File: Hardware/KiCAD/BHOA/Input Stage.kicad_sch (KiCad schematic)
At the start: 15 parts, among them U601 OPA1688, U602 LME49724

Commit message: added outpout relays
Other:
- company: (none) -> C Audio
- title: (none) -> BHOA
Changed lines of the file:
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@@
 (kicad_sch (version 20230121) (generator eeschema)
-  (paper "A5")
+  (paper "A4")
+  (title_block
+    (title "BHOA")
+    (rev "0.1")
+    (company "C Audio")
+    (comment 3 "Balanced Headphone Operationsal Amplifier")
+  )
   (junction (at 126.365 47.625) (diameter 0) (color 0 0 0 0)
   )

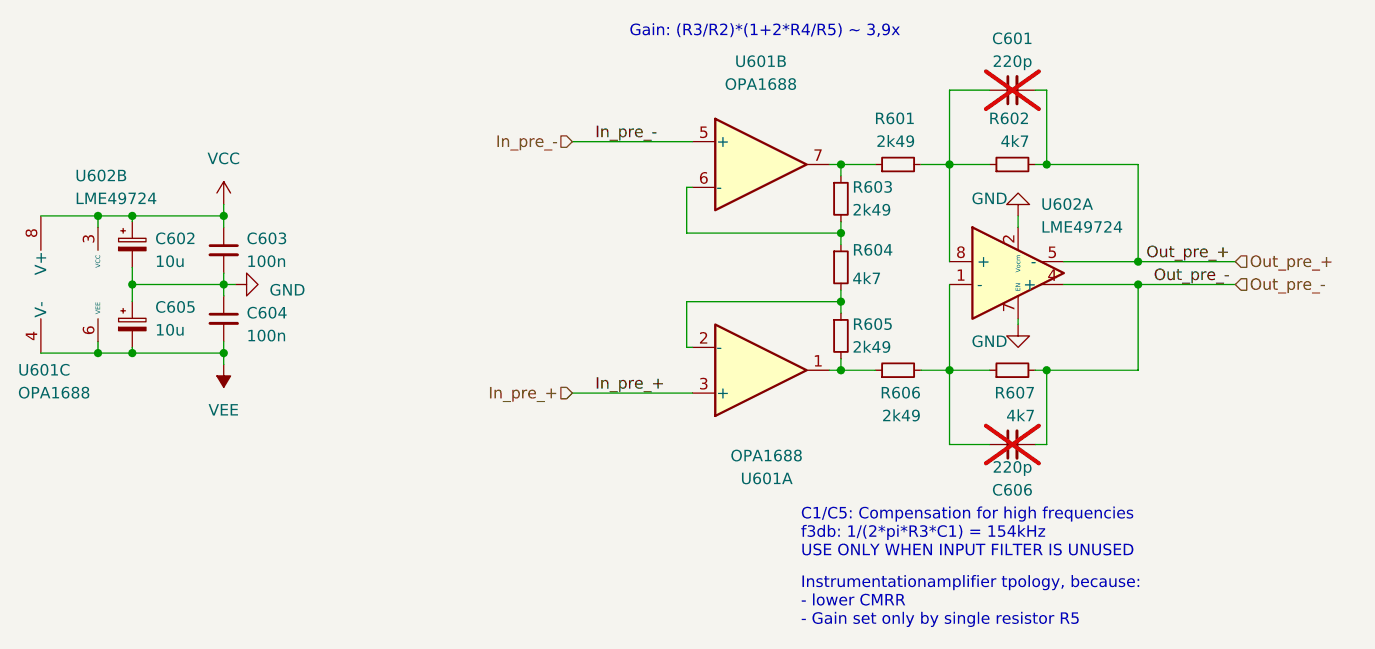
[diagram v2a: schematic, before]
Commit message: Updated PCB with output protection
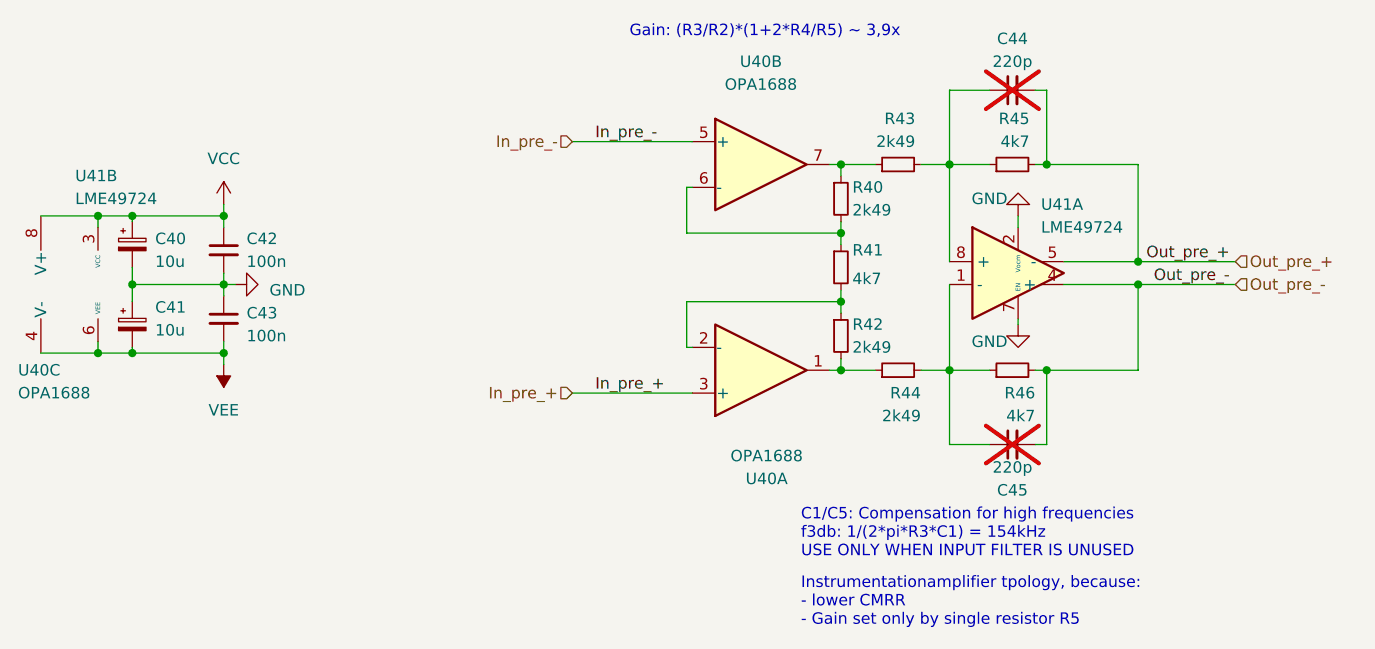
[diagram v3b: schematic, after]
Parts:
- renumbered C602 to C40, C605 to C41, C603 to C42, C604 to C43, C601 to C44, C606 to C45, R603 to R40, R604 to R41, R605 to R42, R601 to R43, R606 to R44, R602 to R45, R607 to R46, U601 to U40, U602 to U41
